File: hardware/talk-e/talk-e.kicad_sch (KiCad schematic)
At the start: 33 parts, among them Q1 FS8205A, SW4 SS-12D00-G 4 E, SW5 SW_Push, U2 DW01A, U3 TP4056-42-ESOP8, U5 AP2112K-3.3

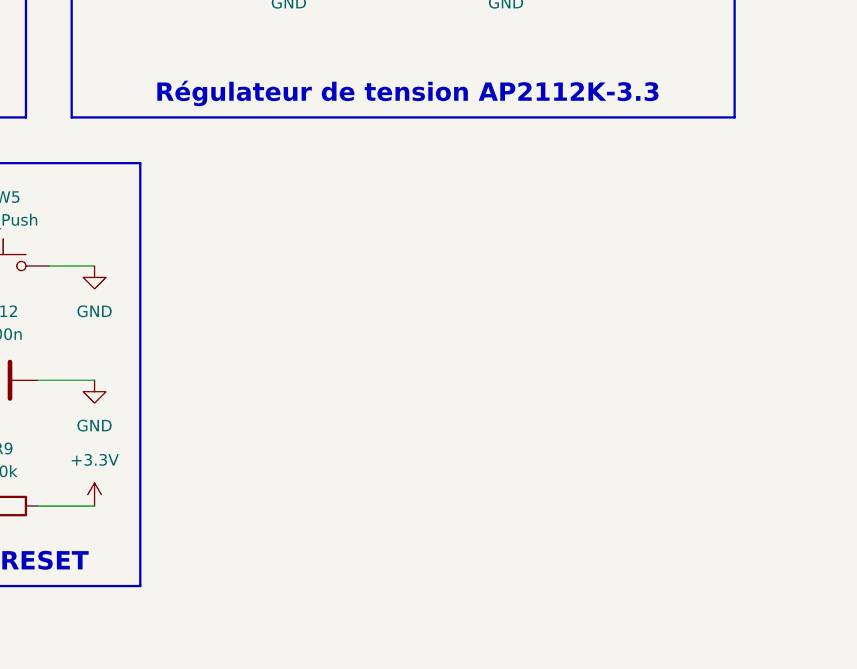
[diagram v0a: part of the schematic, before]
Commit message: add audio components
add audio components
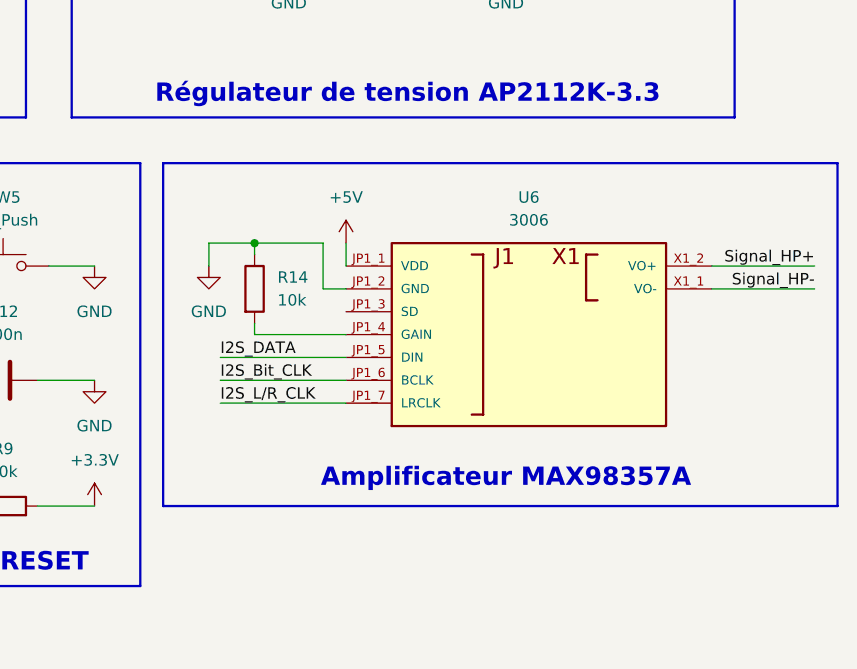
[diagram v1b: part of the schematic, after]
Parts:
- added R14: 10k, symbol Device:R
- added U6: 3006, 3006:MODULE_3006, symbol 3006:3006
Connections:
- net +5V: now also U6.JP1_1 (VDD)
- net GND: now also R14.1, U6.JP1_2 (GND)
- new net: R14.2, U6.JP1_4 (GAIN)
- new net I2S_Bit_CLK: U6.JP1_6 (BCLK)
- new net I2S_DATA: U6.JP1_5 (DIN)
- new net I2S_L/R_CLK: U6.JP1_7 (LRCLK)
- new net Signal_HP+: U6.X1_2 (VO+)
- new net Signal_HP-: U6.X1_1 (VO-)
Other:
- note added: "Amplificateur MAX98357A"

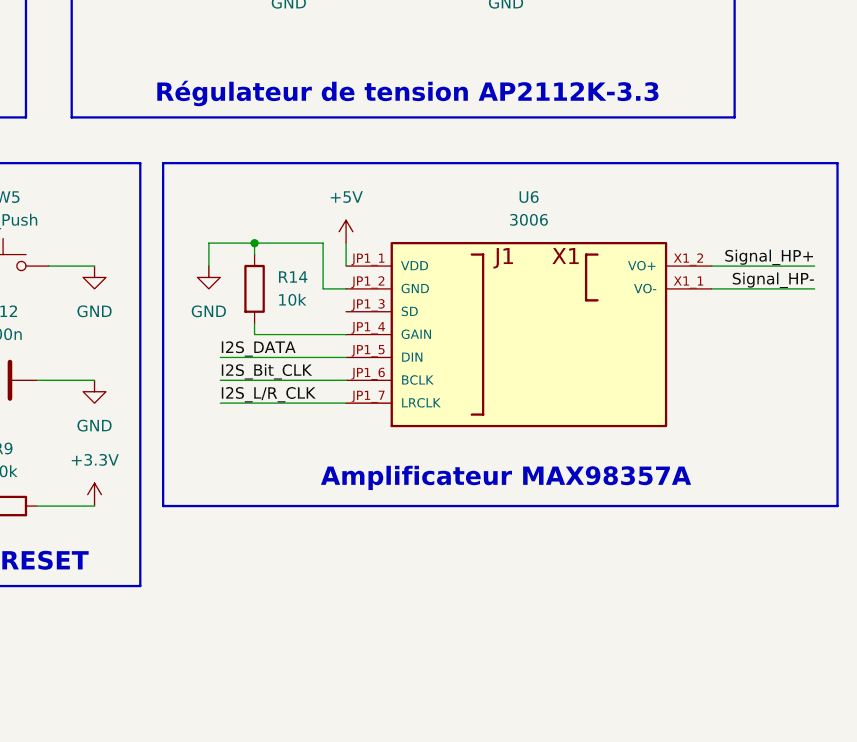
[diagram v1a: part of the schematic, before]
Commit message: Added ampli + mic + finished GPIO mapping
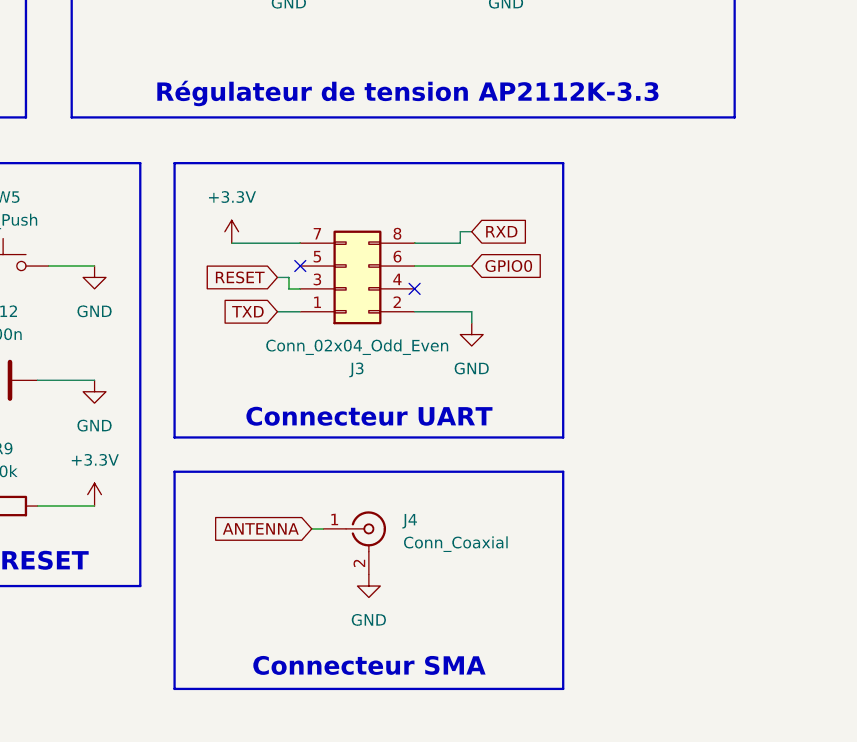
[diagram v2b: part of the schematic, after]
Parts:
- removed R14: 10k, symbol Device:R
- removed U6: 3006, 3006:MODULE_3006, symbol 3006:3006
- added J3: Conn_02x04_Odd_Even, Connector_IDC:IDC-Header_2x04_P2.54mm_Vertical, symbol Connector_Generic:Conn_02x04_Odd_Even
- added J4: Conn_Coaxial, Connector_Coaxial:SMA_Amphenol_901-143_Horizontal, symbol Connector:Conn_Coaxial
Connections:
- net +3.3V: now also J3.7 (Pin_7)
- net GND: now also J3.2 (Pin_2), J4.2 (Ext)
- net RESET: now also J3.3 (Pin_3)
- new net ANTENNA: J4.1 (In)
- new net GPIO0: J3.6 (Pin_6)
- new net RXD: J3.8 (Pin_8)
- new net TXD: J3.1 (Pin_1)
- no-connect marks 3 -> 5
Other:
- note added: "Connecteur SMA"
- note added: "Connecteur UART"
- note removed: "Amplificateur MAX98357A"

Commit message: Finished routing + PCB ready for production
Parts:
- removed C18, C20, C24, C26: 100n, symbol Device:C
- removed C19, C21, C23, C25, C27: 10µ, symbol Device:C
- removed D1: LED, LED_THT:LED_D3.0mm, symbol Device:LED
- removed J3: Conn_02x04_Odd_Even, Connector_IDC:IDC-Header_2x04_P2.54mm_Vertical, symbol Connector_Generic:Conn_02x04_Odd_Even
- removed R2: 1k, symbol Device:R
- removed SW4: SS-12D00-G 4 E, 1P2T_SS-12D00_CNK, symbol 2026-05-09_16-09-49:SS-12D00-G_4_E
- added BOOT1: SW_Push, Button_Switch_THT:SW_PUSH_6mm, symbol Switch:SW_Push
- added D2: 1N5819, Diode_THT:D_DO-41_SOD81_P10.16mm_Horizontal, symbol Diode:1N5819
- added J12: Conn_01x02_Socket, Connector_JST:JST_EH_B2B-EH-A_1x02_P2.50mm_Vertical, symbol Connector:Conn_01x02_Socket
- added J14: Conn_02x04_Odd_Even, Connector_PinHeader_2.54mm:PinHeader_2x04_P2.54mm_Horizontal, symbol Connector_Generic:Conn_02x04_Odd_Even
- added J15: USB_B_Micro, Connector_USB:USB_Micro-AB_Molex_47590-0001, symbol Connector:USB_B_Micro
- added J8: Conn_01x03_Socket, Connector_JST:JST_EH_B3B-EH-A_1x03_P2.50mm_Vertical, symbol Connector:Conn_01x03_Socket
- added J9: Conn_01x02, Connector_JST:JST_EH_B2B-EH-A_1x02_P2.50mm_Vertical, symbol Connector_Generic:Conn_01x02
- added Q2: IRLML6402, Package_TO_SOT_SMD:SOT-23, symbol Transistor_FET:IRLML6402
- added R10: 100k, Resistor_SMD:R_1206_3216Metric, symbol Device:R
- added R15: 330R, Resistor_SMD:R_1206_3216Metric, symbol Device:R
- added R16: 10k, Resistor_SMD:R_1206_3216Metric, symbol Device:R
- added R8: 1k, Resistor_SMD:R_1206_3216Metric, symbol Device:R
- added U3: SBR130S3-7, SBR130S3-7:SBR130S3-7, symbol SBR130S3-7:SBR130S3-7
- C10, C22: footprint (none) -> Capacitor_SMD:C_0805_2012Metric; KiLib_Generator (none) -> SMD_2terminal_chip_molded
- C11: renamed from C16; footprint (none) -> Capacitor_SMD:C_0805_2012Metric; KiLib_Generator (none) -> SMD_2terminal_chip_molded
- C12: renamed from C2; footprint (none) -> Capacitor_SMD:C_0805_2012Metric; KiLib_Generator (none) -> SMD_2terminal_chip_molded
- C13: renamed from C1; footprint (none) -> Capacitor_SMD:C_0805_2012Metric; KiLib_Generator (none) -> SMD_2terminal_chip_molded
- C14: renamed from C3; footprint (none) -> Capacitor_SMD:C_0805_2012Metric; KiLib_Generator (none) -> SMD_2terminal_chip_molded
- C15: renamed from C13; footprint (none) -> Capacitor_SMD:C_0805_2012Metric; KiLib_Generator (none) -> SMD_2terminal_chip_molded
- C16: renamed from C14; footprint (none) -> Capacitor_SMD:C_0805_2012Metric; KiLib_Generator (none) -> SMD_2terminal_chip_molded
- C19: renamed from C15; footprint (none) -> Capacitor_SMD:C_0805_2012Metric; KiLib_Generator (none) -> SMD_2terminal_chip_molded
- C21: renamed from C12; footprint (none) -> Capacitor_SMD:C_0805_2012Metric; KiLib_Generator (none) -> SMD_2terminal_chip_molded
- R11: renamed from R1; value 100 -> 100R; footprint (none) -> Resistor_SMD:R_1206_3216Metric; KiLib_Generator (none) -> SMD_2terminal_chip_molded
- R12: renamed from R5; footprint (none) -> Resistor_SMD:R_1206_3216Metric; KiLib_Generator (none) -> SMD_2terminal_chip_molded
- R13: value 100k -> 10k; footprint (none) -> Resistor_SMD:R_1206_3216Metric; KiLib_Generator (none) -> SMD_2terminal_chip_molded
- R14: renamed from R12; footprint (none) -> Resistor_SMD:R_1206_3216Metric; KiLib_Generator (none) -> SMD_2terminal_chip_molded
- R4: renamed from R9; footprint (none) -> Resistor_SMD:R_1206_3216Metric; KiLib_Generator (none) -> SMD_2terminal_chip_molded
- R9: renamed from R3; value 1.2k -> 1k; footprint (none) -> Resistor_SMD:R_1206_3216Metric; KiLib_Generator (none) -> SMD_2terminal_chip_molded
- RESET1: renamed from SW5; footprint (none) -> Button_Switch_THT:SW_PUSH_6mm
- U2: renamed from U3; KiLib_Generator (none) -> package/gullwing
- U4: renamed from U2; KiLib_Generator (none) -> package/gullwing
- U5: KiLib_Generator (none) -> package/gullwing
- renumbered J4 to J1, Q1 to Q3
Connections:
- net +3.3V: now also R13.1, J14.7 (Pin_7), R15.1, R16.2; no longer C22.2
- net +5V: now also D2.1 (K), Q2.1 (G), R10.2, U3.A
- net B+: now also J9.2 (Pin_2), Q2.3 (D); no longer C14.1, C15.1, U5.1 (VIN), U5.3 (EN)
- net B-: now also J9.1 (Pin_1)
- net CHRG: now also J12.2 (Pin_2)
- net GND: now also C22.2, BOOT1.2, J14.2 (Pin_2), J15.5 (GND), J15.SH (Shield), J8.1 (Pin_1), R10.1, R8.2; no longer C22.1, R13.1, R9.2
- net GPIO0: now also C22.1, BOOT1.1, J14.6 (Pin_6), R16.1
- net RESET: now also J14.3 (Pin_3)
- net RXD: now also J14.8 (Pin_8)
- net SW_LOCK: now also J8.2 (Pin_2)
- net TXD: now also J14.1 (Pin_1)
- net unconnected-(Q2-Pad1)_1: now reaches Q3.1, Q3.8
- new net: J12.1 (Pin_1), R15.2
- new net: R8.1, R9.2
- new net OUT+: C14.1, C15.1, Q2.2 (S), U3.C, U5.1 (VIN), U5.3 (EN)
- new net VBUS: D2.2 (A), J15.1 (VBUS)
- no-connect marks 5 -> 8
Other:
- note added: "580 mA charge"
- note added: "Bouton BOOT"
- note added: "Connecteur USB"
- note added: "Connecteur batterie"
- note added: "D"
- note added: "Diode de protection Évite tout retour de courant"
- note added: "Déconnexion de charge pendant la charge"
- note added: "G"
- note added: "On met le drain vers la batterie, la source vers la charge Pourquoi cette orientation ? 1. Sans alim USB (juste batterie) -> Rpull tire la grille à 0V -> La batterie met la source à Vbat via le drain -> Vgs est négatif donc le PMOS conduit -> La diode de corps est court-circuitée par le canal conducteur 2. Avec alim USB (5V) -> La grille est tirée à 5V -> La sourc eest à 4.6V (après la diode Scho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"
- note added: "S"
- note removed: "Découplage des alimentations du MCU"
- note removed: "Rajouter USB (remplacer port USB)"
- note removed: "Rajouter connecteur batterie"
- moved on the sheet: C10, C11, C12, C13, C14, C15, C16, C19, C21, J1, Q3, R11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
